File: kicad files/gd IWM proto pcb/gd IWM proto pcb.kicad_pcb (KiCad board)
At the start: 2 copper layers, 88.9 x 54.6 mm, 65 parts, among them J1 DB19_4, J10 CPx_LA, J11 Addr, J12 SW_LA, J13 Game Port, J14 Data, J15 IWM-LA, J16 FDC Hdr, J17 EN, J18 Ctrl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

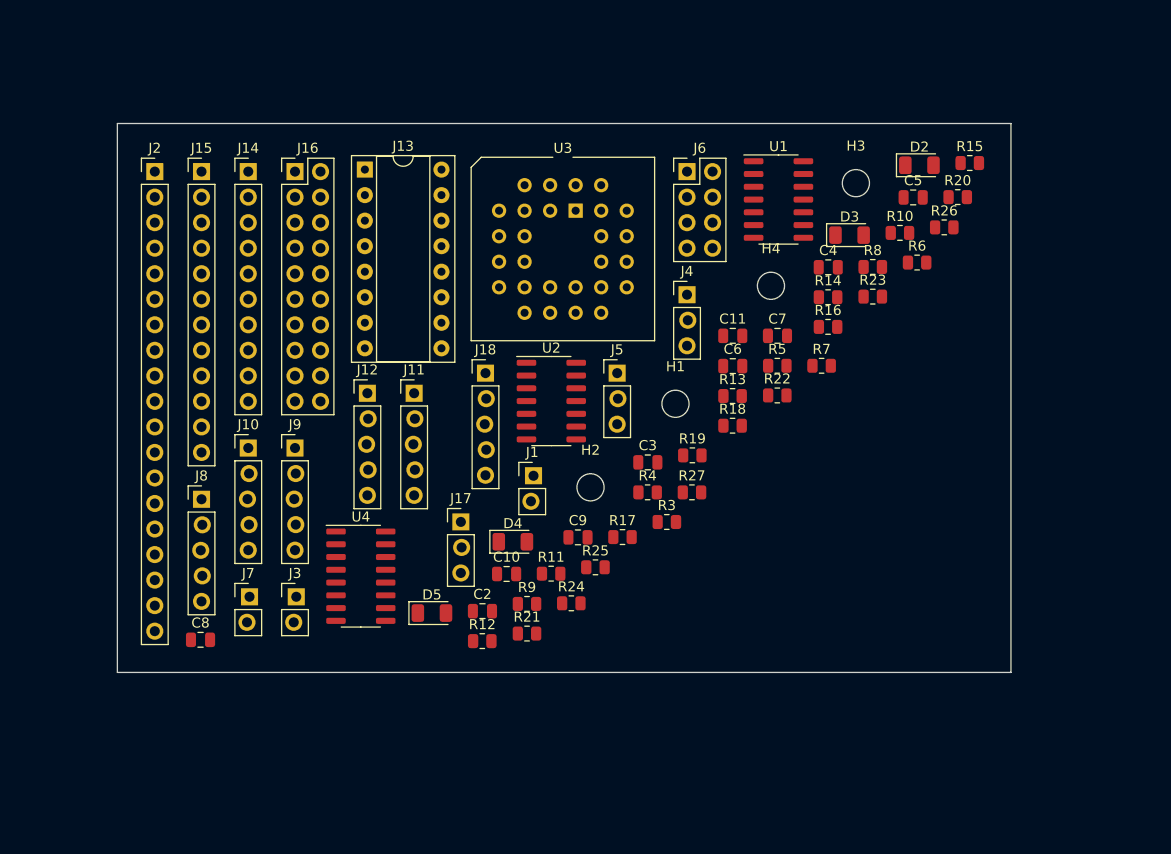
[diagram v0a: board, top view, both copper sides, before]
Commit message: created DSUB19 footprint and initial layout of IWM board (with some initial trace ideas)
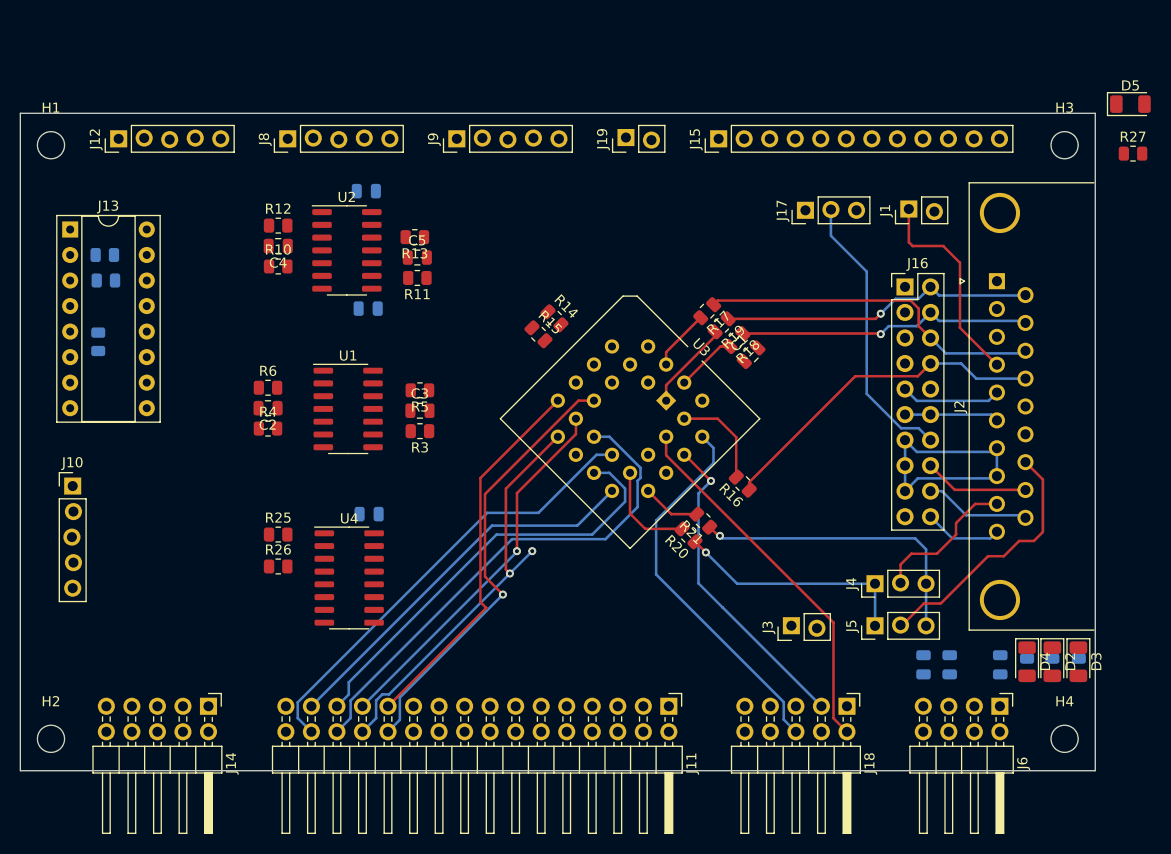
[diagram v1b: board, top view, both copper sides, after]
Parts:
- removed J7: PDL_LA, My Libraries:PinHeader_1x02_P2.54mm_Vertical-LOCK
- added C1: 10u, Capacitor_SMD:C_0805_2012Metric, F.Cu at (173.5, 91.6)
- added J19: Slot_Maker, My Libraries:PinHeader_1x02_P2.54mm_Vertical-LOCK, F.Cu at (161.1, 70.1)
- C10, C11, C6, C7, C8, C9, R22, R23, R24, R7, R8, R9: moved to B.Cu
- D2: value -5d -> -5v
- D3: value +5d -> +5v
- D4: value +12d -> +12v
- J11: value Addr -> Addr_Main_Data; footprint My Libraries:PinHeader_1x05_P2.54mm_Vertical-LOCK -> Connector_PinHeader_2.54mm:PinHeader_2x16_P2.54mm_Horizontal
- J14: value Data -> CTRL2; footprint Connector_PinHeader_2.54mm:PinHeader_1x10_P2.54mm_Vertical -> Connector_PinHeader_2.54mm:PinHeader_2x05_P2.54mm_Horizontal
- J18: value Ctrl -> CTRL1; footprint My Libraries:PinHeader_1x05_P2.54mm_Vertical-LOCK -> Connector_PinHeader_2.54mm:PinHeader_2x05_P2.54mm_Horizontal
- J2: value DB19 -> DSUB19; footprint Connector_PinHeader_2.54mm:PinHeader_1x19_P2.54mm_Vertical -> My Libraries:DSUB-19_Apple_II_Floppy
- J6: footprint Connector_PinHeader_2.54mm:PinHeader_2x04_P2.54mm_Vertical -> Connector_PinHeader_2.54mm:PinHeader_2x04_P2.54mm_Horizontal
- moved D5 86.0 mm to (211.3, 66.6)
- moved J2 84.5 mm to (198.0, 84.3), turned to 90 degrees
- moved C8 79.6 mm to (198.3, 122.4), turned to 90 degrees
- moved R23 76.3 mm to (109.3, 84.2)
- moved R26 74.4 mm to (126.5, 112.6)
- moved R22 67.8 mm to (108.6, 90.3), turned to 90 degrees
- moved H1 67.2 mm to (103.9, 70.7)
- moved R6 65.8 mm to (125.5, 94.9)
- moved R10 61.9 mm to (126.5, 82.8)
- moved J16 61.8 mm to (188.8, 84.8)
- moved J6 61.6 mm to (198.3, 126.6), turned to 270 degrees
- moved H2 59.2 mm to (103.9, 129.8)
- moved R24 57.9 mm to (109.2, 81.7)
- moved R27 55.3 mm to (211.5, 71.6)
- moved C4 54.8 mm to (126.5, 80.8), turned to 180 degrees
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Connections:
- J11 pad 1: /A0 -> GND
- J11 pad 2: /A1 -> GND
- J11 pad 3: /A2 -> /BA1
- J11 pad 4: /A3 -> /BA0
- J11 pad 5: GND -> /BA3
- J12 pad 1: /SW0_OAPL -> /SW2
- J12 pad 3: /SW2 -> /SW0_OAPL
- J14 pad 1: /MDBUS0 -> Net-(J14-Pad1)
- J14 pad 2: /MDBUS1 -> /C060-67
- J14 pad 3: /MDBUS2 -> Net-(J14-Pad3)
- J14 pad 4: /MDBUS3 -> Net-(J14-Pad4)
- J14 pad 5: GND -> Net-(J14-Pad5)
- J14 pad 6: /MDBUS4 -> Net-(J14-Pad6)
- J14 pad 7: /MDBUS5 -> /PDLTRIG
- J14 pad 8: /MDBUS6 -> Net-(J14-Pad8)
- J14 pad 9: /MDBUS7 -> GND
- J18 pad 1: /Q3 -> Net-(J18-Pad1)
- J18 pad 3: GND -> /RESET
- J18 pad 4: /RESET -> Net-(J18-Pad4)
- J18 pad 5: /INTDEV6 -> Net-(J18-Pad5)
- U3 pad 10: /MDBUS0 -> /MD0
- U3 pad 11: /MDBUS1 -> /MD1
- U3 pad 12: /MDBUS2 -> /MD2
- U3 pad 13: /MDBUS3 -> /MD3
- U3 pad 15: /MDBUS4 -> /MD4
- U3 pad 16: /MDBUS5 -> /MD5
- U3 pad 17: /MDBUS6 -> /MD6
- U3 pad 18: /MDBUS7 -> /MD7
- U3 pad 3: /A0 -> /BA0
- U3 pad 4: /A1 -> /BA1
- U3 pad 5: /A2 -> /BA2
- U3 pad 6: /A3 -> /BA3
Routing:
- net /MD4: track 0.00 -> 50.1 mm
- net /MD6: track 0.00 -> 45.0 mm
- net /MD0: track 0.00 -> 43.8 mm, vias 0 -> 1
- net /MD5: track 0.00 -> 42.9 mm
- net /MD2: track 0.00 -> 41.3 mm, vias 0 -> 2
- net /MD7: track 0.00 -> 38.8 mm
- net /Q3: track 0.00 -> 37.9 mm
- net /MD1: track 0.00 -> 37.9 mm
- net /MD3: track 0.00 -> 37.4 mm, vias 0 -> 1
- net /7M: track 0.00 -> 36.8 mm
- net /seek2: track 0.00 -> 34.5 mm
- net /seek3: track 0.00 -> 33.8 mm
- net /RESET: track 0.00 -> 31.7 mm, vias 0 -> 1
- net /seek0: track 0.00 -> 31.3 mm, vias 0 -> 1
- net /bEN2: track 0.00 -> 30.1 mm, vias 0 -> 1
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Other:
- board size 88.9 x 54.6 mm -> 106.9 x 65.4 mm
- net class Default: clearance 0.2 -> 0.2032; trace_width 0.25 -> 0.254
- rule trace_clearance: 0.2 -> 0.2032

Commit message: removed mounting holes. changed LA headers to 2x connectors. planning to reduce overall space.
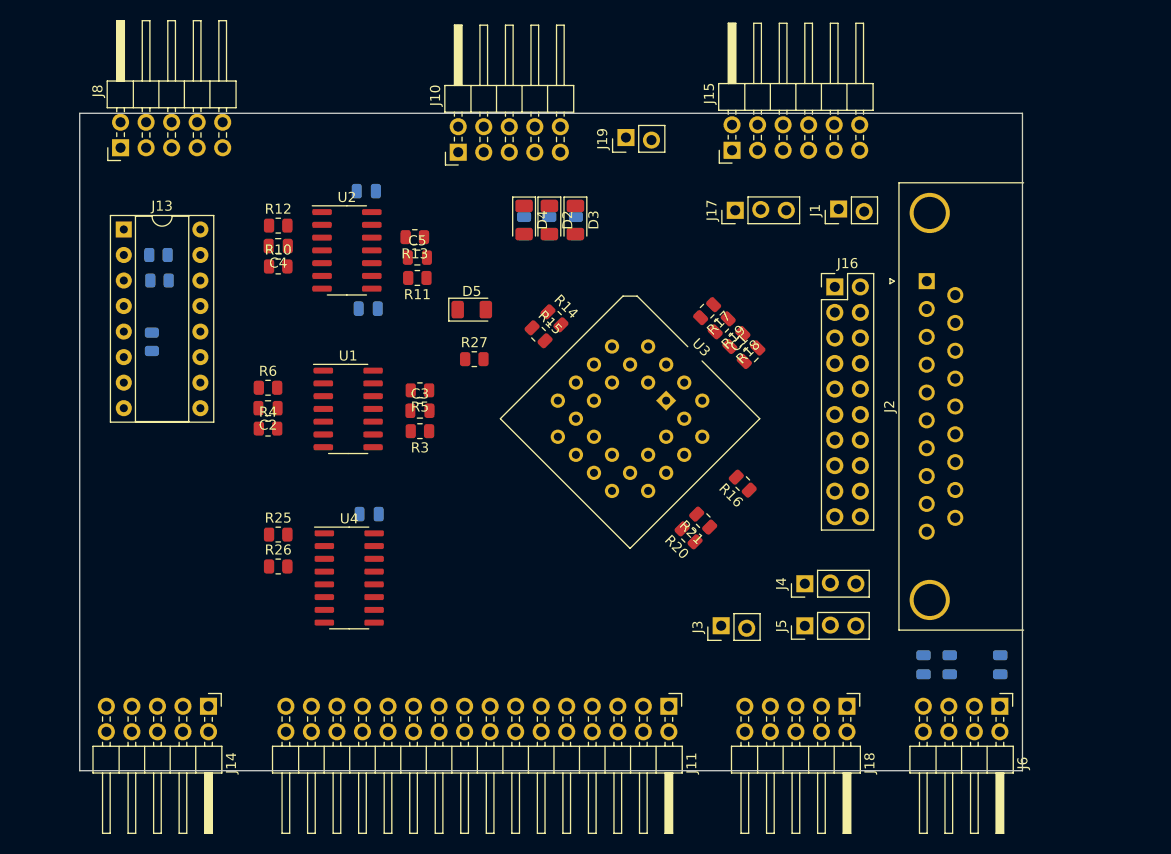
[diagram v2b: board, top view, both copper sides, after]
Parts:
- removed H1, H2, H3, H4: MountingHole_M2.5_Screw, MountingHole:MountingHole_2.7mm_M2.5
- removed J12: SW_LA, My Libraries:PinHeader_1x05_P2.54mm_Vertical-LOCK
- removed J9: PDx_LA, My Libraries:PinHeader_1x05_P2.54mm_Vertical-LOCK
- J10: footprint My Libraries:PinHeader_1x05_P2.54mm_Vertical-LOCK -> Connector_PinHeader_2.54mm:PinHeader_2x05_P2.54mm_Horizontal
- J15: footprint Connector_PinHeader_2.54mm:PinHeader_1x12_P2.54mm_Vertical -> Connector_PinHeader_2.54mm:PinHeader_2x06_P2.54mm_Horizontal
- J8: value DIS_LA -> 555_LA; footprint My Libraries:PinHeader_1x05_P2.54mm_Vertical-LOCK -> Connector_PinHeader_2.54mm:PinHeader_2x05_P2.54mm_Horizontal
- moved R27 68.6 mm to (146.0, 92.0)
- moved D5 68.6 mm to (145.7, 87.1)
- moved R7 66.6 mm to (156.1, 78.8)
- moved D2 66.6 mm to (153.5, 78.2)
- moved D3 66.6 mm to (156.1, 78.2)
- moved D4 66.6 mm to (151.0, 78.2)
- moved R8 66.6 mm to (151.0, 78.8)
- moved R9 66.6 mm to (153.5, 78.8)
- moved J10 50.7 mm to (144.4, 71.4), turned to 90 degrees
- moved J8 16.7 mm to (110.8, 71.0)
- moved J17 6.99 mm to (172.0, 77.2)
- moved J1 6.98 mm to (182.2, 77.2)
- moved J16 6.98 mm to (181.9, 84.8)
- moved J2 6.98 mm to (191.0, 84.3)
- moved J3 6.98 mm to (170.6, 118.7)
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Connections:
- J10 pad 2: /CP1 -> /SW2
- J10 pad 3: /CP2 -> /CP1
- J10 pad 4: /CP3 -> /SW1_CAPL
- J10 pad 5: GND -> /CP2
- J15 pad 10: GND -> /EN1
- J15 pad 11: /EN1 -> /PHd
- J15 pad 2: /RDATA -> /PHc
- J15 pad 3: /WDATA -> /RDATA
- J15 pad 4: /WREQ -> /PHb
- J15 pad 5: GND -> /WDATA
- J15 pad 6: /PHd -> /PHa
- J15 pad 7: /PHc -> /WREQ
- J15 pad 8: /PHb -> GND
- J15 pad 9: /PHa -> GND
- J8 pad 2: /DIS1 -> /PDL0
- J8 pad 3: /DIS2 -> /DIS1
- J8 pad 4: /DIS3 -> /PDL1
- J8 pad 5: GND -> /DIS2
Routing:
- net /MD4: track 50.1 -> 0.00 mm
- net /MD6: track 45.0 -> 0.00 mm
- net /MD0: track 43.8 -> 0.00 mm, vias 1 -> 0
- net /MD5: track 42.9 -> 0.00 mm
- net /MD2: track 41.3 -> 0.00 mm, vias 2 -> 0
- net /MD7: track 38.8 -> 0.00 mm
- net /Q3: track 37.9 -> 0.00 mm
- net /MD1: track 37.9 -> 0.00 mm
- net /MD3: track 37.4 -> 0.00 mm, vias 1 -> 0
- net /7M: track 36.8 -> 0.00 mm
- net /seek2: track 34.5 -> 0.00 mm
- net /seek3: track 33.8 -> 0.00 mm
- net /RESET: track 31.7 -> 0.00 mm, vias 1 -> 0
- net /seek0: track 31.3 -> 0.00 mm, vias 1 -> 0
- net /bEN2: track 30.1 -> 0.00 mm, vias 1 -> 0
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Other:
- board size 106.9 x 65.4 mm -> 93.8 x 65.4 mm

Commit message: routed most of critical signals. now trying to get LA headers
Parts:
- R27: moved to B.Cu
- moved J19 32.8 mm to (130.4, 81.7), turned to 270 degrees
- moved J1 20.0 mm to (164.8, 87.0), turned to 270 degrees
- moved J13 17.7 mm to (109.5, 96.7)
- moved R23 17.6 mm to (113.3, 101.7)
- moved R22 16.6 mm to (113.3, 106.9), turned to 180 degrees
- moved R24 15.0 mm to (113.3, 96.6)
- moved C9 14.5 mm to (135.4, 101.5)
- moved C1 14.4 mm to (174.8, 105.9), turned to 315 degrees
- moved C10 13.9 mm to (135.4, 89.3)
- moved J8 13.9 mm to (111.1, 84.9)
- moved R10 13.7 mm to (126.5, 96.5)
- moved J15 13.7 mm to (171.9, 84.9)
- moved R27 13.6 mm to (136.5, 82.2), turned to 90 degrees
- moved J10 13.5 mm to (144.7, 84.9)
- moved J17 12.6 mm to (171.3, 89.8)
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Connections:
- J2 pad 16: /DB19-4 -> /DB19-16
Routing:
- net +5V: track 0.00 -> 186.3 mm, vias 0 -> 4
- net +12V: track 0.00 -> 109.6 mm, vias 0 -> 2
- net -12V: track 0.00 -> 103.2 mm, vias 0 -> 1
- net /bWREQ: track 0.00 -> 56.4 mm, vias 0 -> 1
- net /bWDATA: track 0.00 -> 55.4 mm, vias 0 -> 1
- net /DB19-16: track 0.00 -> 47.5 mm, vias 0 -> 1
- net /MD6: track 0.00 -> 44.1 mm
- net /DB19-4: track 0.00 -> 44.0 mm
- net /RDATA: track 0.00 -> 40.5 mm, vias 0 -> 1
- net /seek2: track 0.00 -> 38.4 mm
- net /RESET: track 0.00 -> 37.9 mm, vias 0 -> 1
- net /BA2: track 0.00 -> 37.7 mm
- net /MD4: track 0.00 -> 37.7 mm, vias 0 -> 1
- net /MD7: track 0.00 -> 35.7 mm
- net /MD3: track 0.00 -> 34.1 mm, vias 0 -> 1
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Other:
- board size 93.8 x 65.4 mm -> 93.2 x 54.7 mm
- net class Power added: clearance 0.1524, trace_width 0.3556, via_dia 0.8, via_drill 0.4

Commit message: finished IWM pcb rev1
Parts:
- added REF**: KiCad-Logo2_5mm_SilkScreen, Symbol:KiCad-Logo2_5mm_SilkScreen, B.Cu at (127.8, 94.8)
- added REF**: OSHW-Symbol_6.7x6mm_SilkScreen, Symbol:OSHW-Symbol_6.7x6mm_SilkScreen, F.Cu at (119.5, 91.9)
- added svg2mod: G***, My Libraries:BE5v2, F.Cu at (141.8, 113.5)
- moved J1 0.59 mm to (165.2, 87.4)
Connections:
- J15 pad 10: /EN1 -> /bEN1
- J15 pad 11: /PHd -> /seek3
- J15 pad 12: /EN2 -> /bEN2
- J15 pad 2: /PHc -> /seek2
- J15 pad 4: /PHb -> /seek1
- J15 pad 6: /PHa -> /seek0
- U4 pad 10: /A1 -> /BA1
- U4 pad 11: /A0 -> /BA0
- U4 pad 5: /MDBUS7 -> /MD7
- U4 pad 9: /A2 -> /BA2
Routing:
- net /bEN1: track 0.00 -> 122.8 mm, vias 0 -> 6
- net /SW0_OAPL: track 0.00 -> 106.3 mm
- net /SW1_CAPL: track 0.00 -> 98.4 mm, vias 0 -> 1
- net /SW2: track 0.00 -> 94.7 mm, vias 0 -> 2
- net /bEN2: track 0.00 -> 92.0 mm, vias 0 -> 5
- net /SW3: track 0.00 -> 87.6 mm, vias 0 -> 6
- net /SENSE: track 31.2 -> 105.5 mm, vias 2 -> 3
- net /DiskAct: track 0.00 -> 68.2 mm, vias 0 -> 4
- net /CP2: track 0.00 -> 63.8 mm, vias 0 -> 1
- net /PDL1: track 0.00 -> 60.3 mm, vias 0 -> 4
- net /PDL3: track 0.00 -> 57.4 mm
- net /PDLTRIG: track 0.00 -> 55.1 mm, vias 0 -> 2
- net +5V: track 186.3 -> 241.1 mm, vias 4 -> 9
- net /CP0: track 0.00 -> 54.1 mm, vias 0 -> 5
- net /CP3: track 0.00 -> 51.9 mm, vias 0 -> 1
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- added copper zone on B.Cu, net GND
- added copper zone on F.Cu, net GND
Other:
- outline, holes or cut-outs redrawn
- board text added: "+12"
- board text added: "+12V"
- board text added: "+5"
- board text added: "+5V"
- board text added: "-12"
- board text added: "-12V"
- board text added: "0"
- board text added: "1"
- board text added: "10"
- board text added: "11"
- board text added: "12"
- board text added: "13"
- board text added: "15"
- board text added: "16"
- board text added: "17"
- board text added: "18"
- board text added: "19"
- board text added: "2"
- board text added: "21"
- board text added: "23"
- board text added: "3"
- board text added: "4"
- board text added: "5"
- board text added: "6"
- board text added: "7"
- board text added: "7M"
- board text added: "8"
- board text added: "9"
- board text added: "AN0"
- board text added: "AN1"
- board text added: "AN2"
- board text added: "AN3"
- board text added: "BA0 BA1"
- board text added: "BA10 BA11"
- board text added: "BA14 BA15"
- board text added: "BA6 BA7"
- board text added: "C060"
- board text added: "CPL CP1"
- board text added: "DB-16"
- board text added: "DB-4"
- board text added: "DISK"
- board text added: "EN1"
- board text added: "EN2"
- board text added: "GD - IWM Breakout 2021-08-26 @baldengineer"
- board text added: "Gameport"
- board text added: "Header"
- board text added: "INTDEV6"
- board text added: "J10"
- board text added: "J16"
- board text added: "J17"
- board text added: "J2"
- board text added: "J8"
- board text added: "MD1"
- board text added: "MD5"
- board text added: "OPL CP2"
- board text added: "PDL"
- board text added: "PDL --- DIS"
- board text added: "PDL0"
- board text added: "PDL1"
- board text added: "PDL2"
- board text added: "PDL3"
- board text added: "PHa"
- board text added: "PHb"
- board text added: "PHc"
- board text added: "PHd"
- board text added: "Pin17"
- board text added: "Pin9"
- board text added: "SW2 CP0"
- board text added: "SW3"
- board text added: "SW3 CP3"
- board text added: "q3"

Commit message: Changed power connector pinout to make backplane more sensible.
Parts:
- removed REF**: KiCad-Logo2_5mm_SilkScreen, Symbol:KiCad-Logo2_5mm_SilkScreen
- removed REF**: OSHW-Symbol_6.7x6mm_SilkScreen, Symbol:OSHW-Symbol_6.7x6mm_SilkScreen
- removed svg2mod: G***, My Libraries:BE5v2
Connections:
- J6 pad 1: +5V -> GND
- J6 pad 4: GND -> +5V
- J6 pad 6: -12V -> +12V
- J6 pad 7: +12V -> -12V
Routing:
- net +12V: track 114.6 -> 128.5 mm
- net +5V: track 241.1 -> 248.2 mm
- net -12V: track 106.4 -> 107.1 mm
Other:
- board text removed: "+12V"
- board text removed: "+5V"
- board text removed: "-12V"
